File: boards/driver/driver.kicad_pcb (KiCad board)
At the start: 2 copper layers, 50 x 50 mm, 39 parts, among them J1 IN 12V/DATA/GND, J2 OUT 12V/DATA/GND, J3 LED harness, U1 WS2811, U2 PT4115, U3 PT4115, U4 PT4115, U5 78L05, U6 74HC04, U7 74AHCT1G125

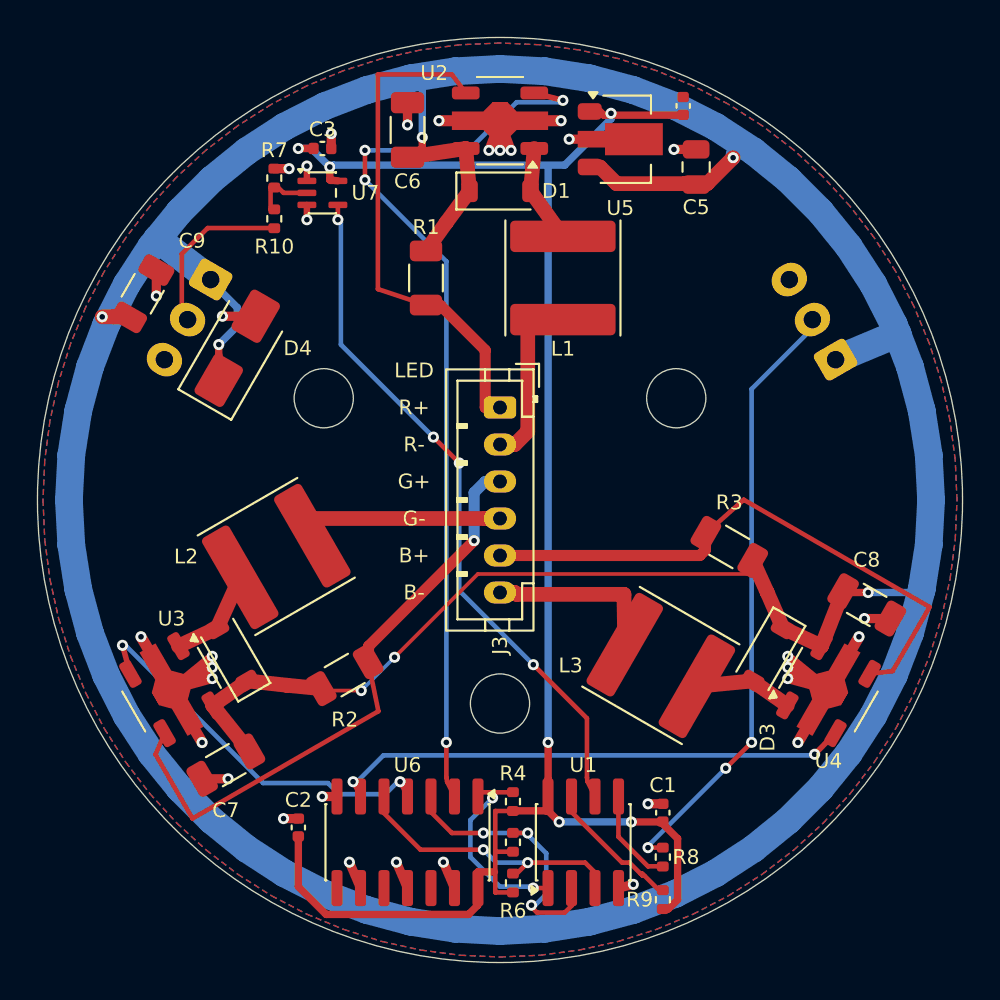
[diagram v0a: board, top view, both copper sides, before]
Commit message: v2: LED channel simulation, pcb-kit checks and docs, open 12 V trunk
sim/channel.py simulates one PT4115 channel in ngspice through pcbkit.spice:
a behavioural PT4115 (hysteretic switch from the datasheet) with the board's
real L, Rs, Schottky, caps and supply cable. Full white is 5.0 W, 0.42 A per
light, 78-83 % efficient, with the Schottky the hottest part. Brightness
tracks the WS2811 PWM within 5 % above 20 % duty and runs bright below that;
the lowest levels fall short. Results in DESIGN.md 2.7 and sim/results/.

pcbkit check on the driver: the 12 V back-layer ring was a closed loop, so
it is now an arc from J1 over the top to the blue cell's tap, and its dead
ends are trimmed. The PWR net class is 0.8 mm (the taps); the 1.5 mm
pass-through is drawn explicitly. DRC 0/0, no stubs or loops; the remaining
thin-feed flags are deliberate and explained in LAYOUT.md.

Docs follow pcb-kit's conventions: LAYOUT.md (the PCB sections from
DESIGN.md), PRODUCTION.md (order files, polarity checklist, harness,
bring-up), status lines, and dated decisions D1-D13 in DESIGN.md. D13: up to
6 lights per 12 V feed.

scripts/make_fab.sh comes from pcb-kit's project template, and the outline
script uses pcbkit.mech.top_level_blocks. The root .bomi and old BOM files
were replaced by the per-board BOMs in the previous commit; their removal is
recorded here.

Co-Authored-By: Claude Opus 5.5 <noreply@anthropic.com>
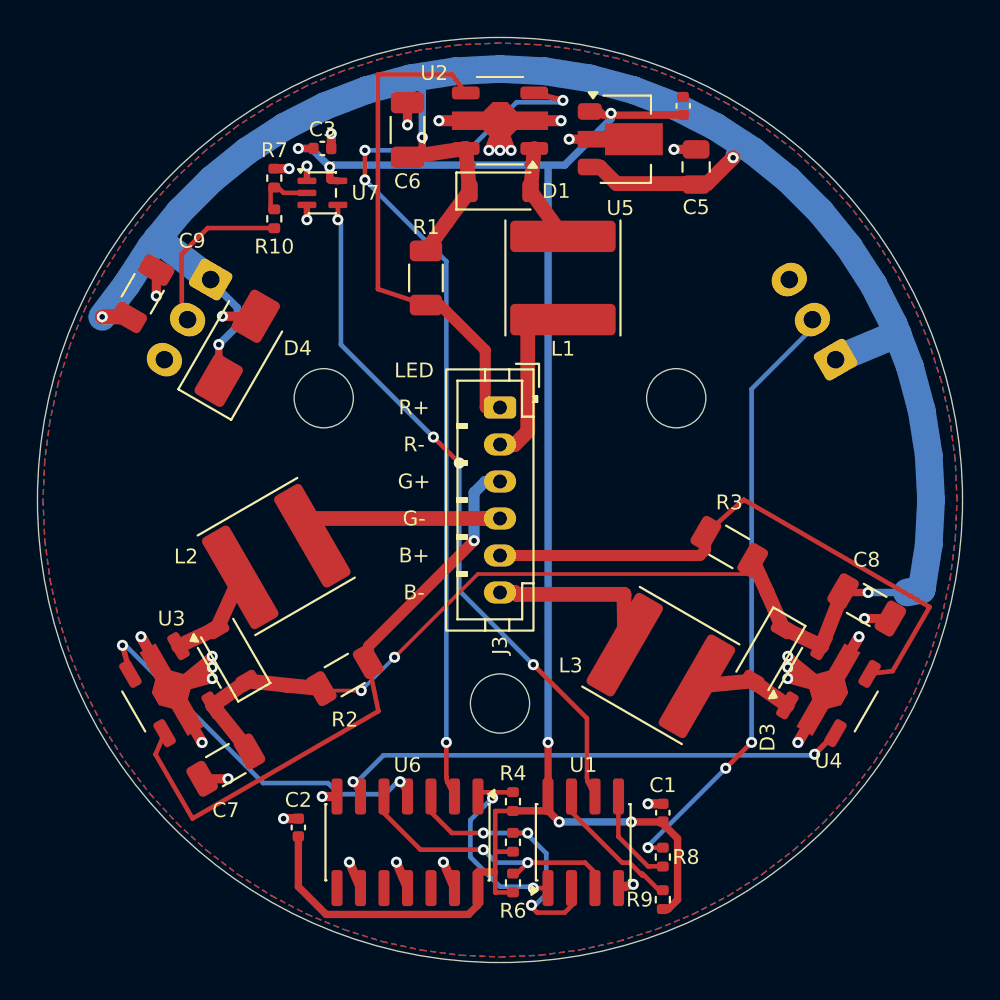
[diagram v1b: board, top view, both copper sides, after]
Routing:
- net +12V: track 233.1 -> 155.6 mm

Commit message: production: adopt pcb-kit's release flow (pcbkit.toml), v2.0 silkscreen labels
- pcbkit.toml: boards/*, JLC files only; pcbkit release --dry-run passes both boards (would release v2.0)
- silkscreen "v2" -> "v2.0" so pcbkit release re-stamps it; LED label moved to r = 12.2 mm to clear H3
- PRODUCTION.md: release/order steps, never-checked SOT-89/SOT-353 rotations, J1/J2 back BOM, overview
- LAYOUT/README/DESIGN: cleanup --dry-run result, release commands

Co-Authored-By: Claude Opus 5.5 <noreply@anthropic.com>
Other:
- board text added: "RGB Spotlight driver v2.0"
- board text removed: "RGB Spotlight driver v2"
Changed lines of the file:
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@@
 		)
 	)
-	(gr_text "RGB Spotlight driver v2"
+	(gr_text "RGB Spotlight driver v2.0"
 		(at 150 115.6 0)
 		(layer "B.SilkS")
